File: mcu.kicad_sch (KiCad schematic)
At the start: 37 parts, among them J17 CAN, J19 Conn_ARM_JTAG_SWD_10, J20 Conn_ARM_JTAG_SWD_10, J21 Conn_01x04_Pin, SW1 RESET, SW2 BOOT, U17 HDC1080, U18 SN65HVD230, U8 STM32G473CBTx, Y1 8 MHz

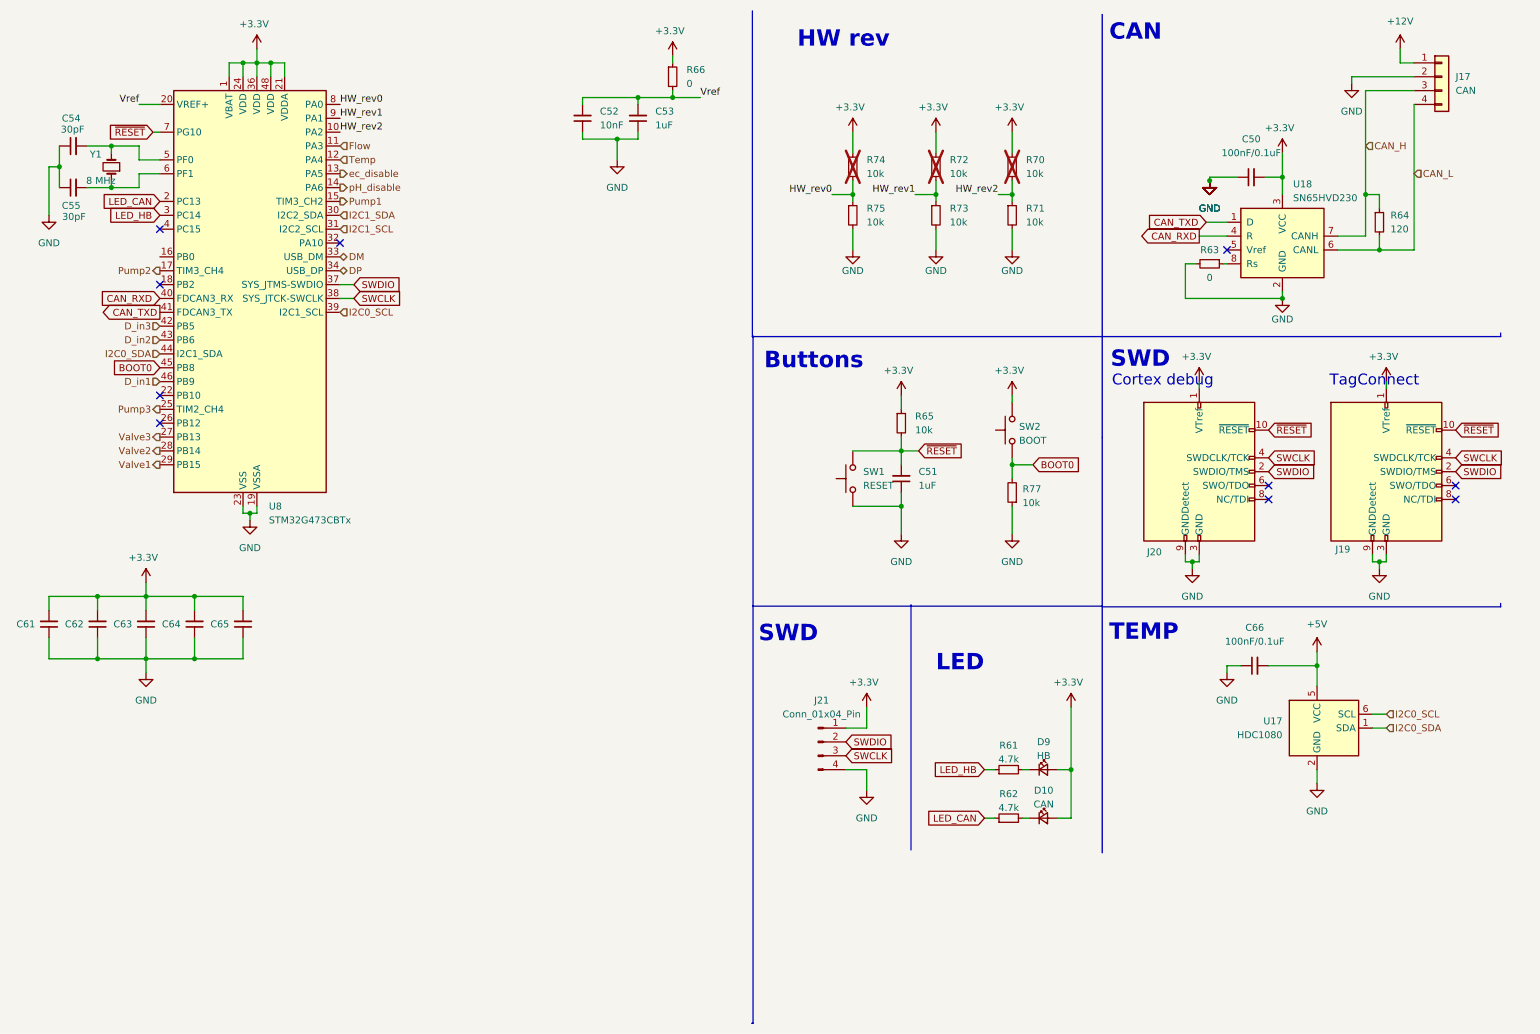
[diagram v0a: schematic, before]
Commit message: Fix ERC warnings
See #28
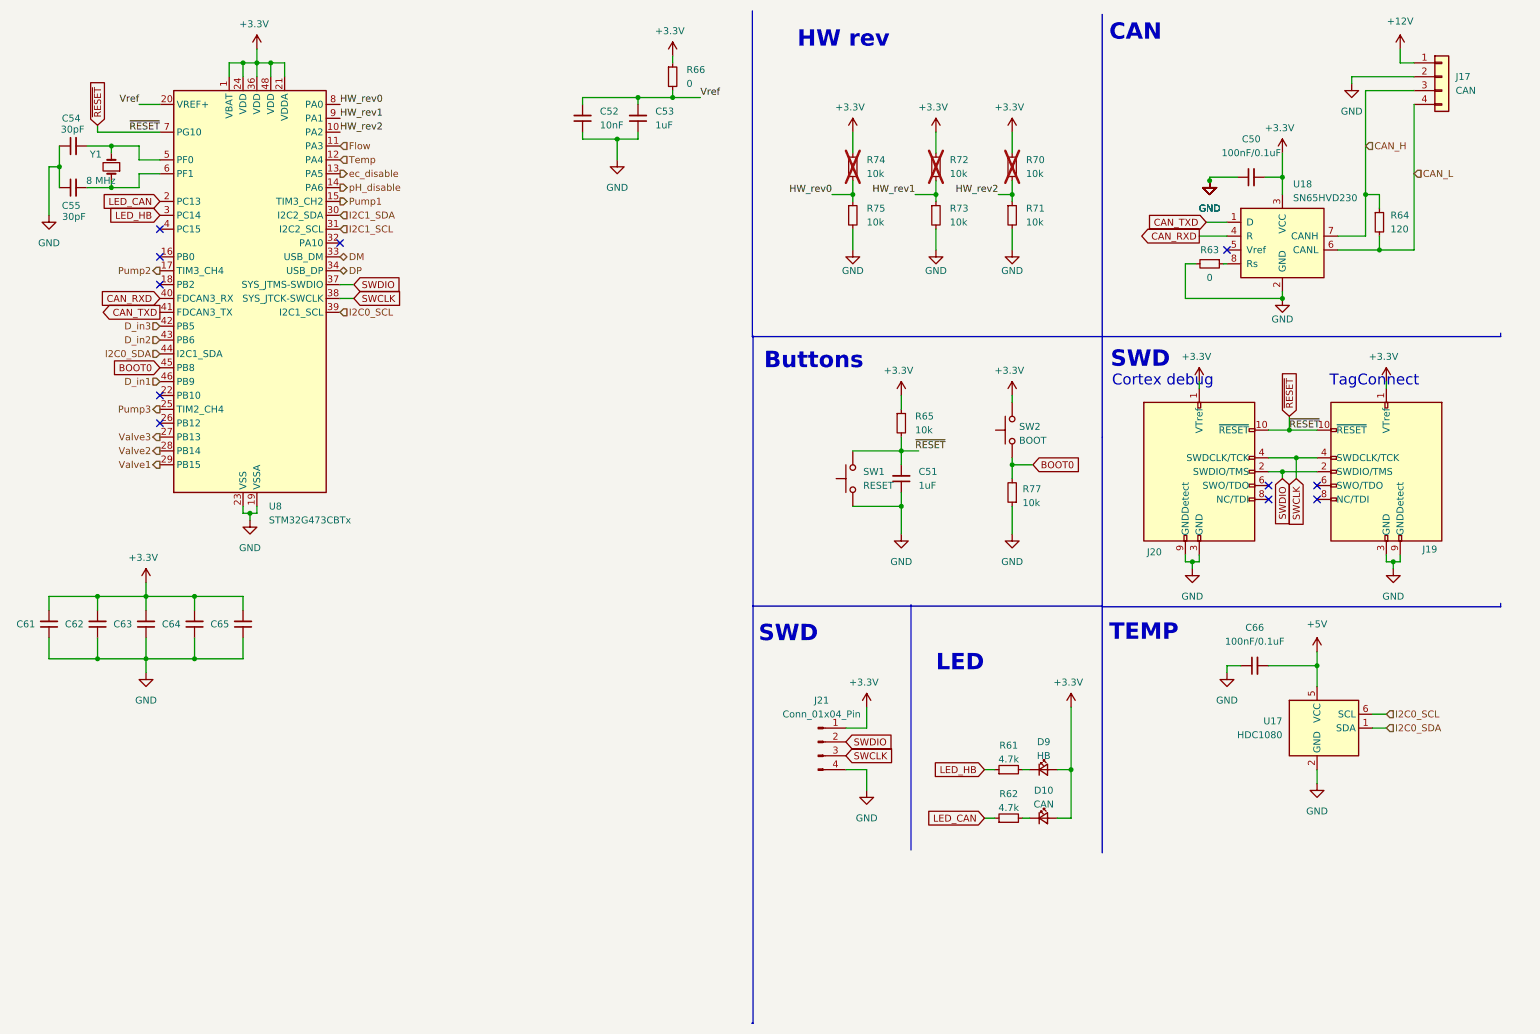
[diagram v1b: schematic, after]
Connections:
- no-connect marks 10 -> 11
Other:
- moved on the sheet: J19

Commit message: Fix ERC errors
Closes #28
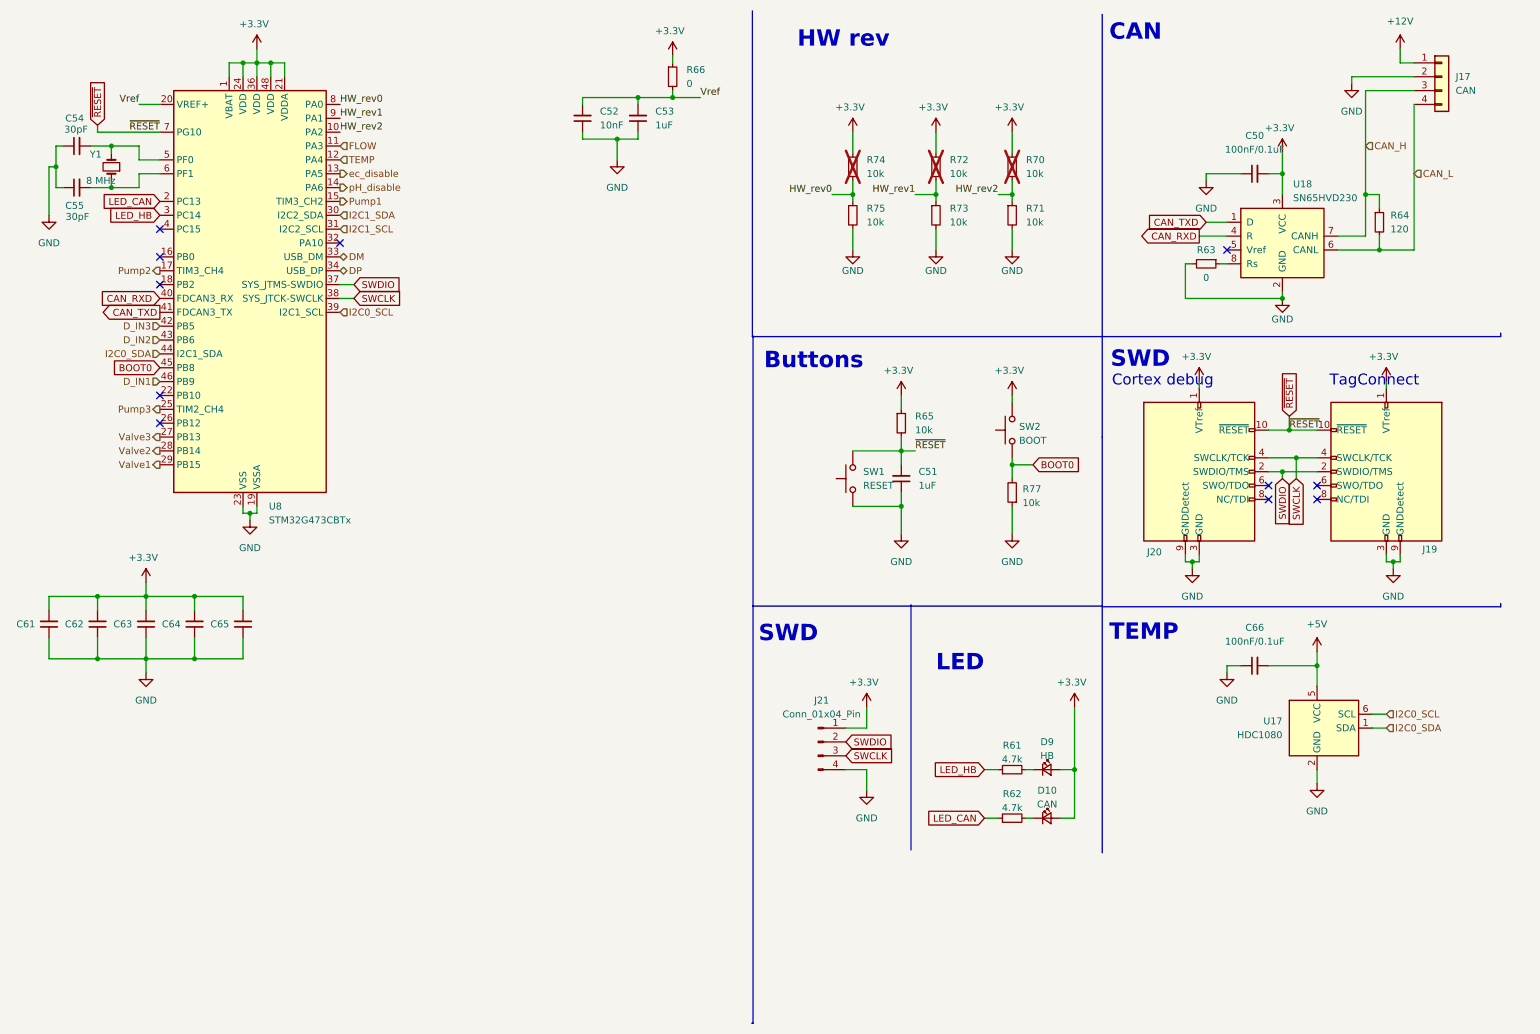
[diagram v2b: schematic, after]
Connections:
- net D_in1 renamed D_IN1
- net D_in2 renamed D_IN2
- net D_in3 renamed D_IN3
- net Flow renamed FLOW
- net Temp renamed TEMP
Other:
- moved on the sheet: C50, C54, C55, D10, D9, R61, R62, R63

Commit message: Bump HW rev
Closes #43
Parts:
- R74: now fitted; now in the parts list
- R75: now not fitted; now left out of the parts list
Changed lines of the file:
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@@
 		(unit 1)
 		(exclude_from_sim no)
-		(in_bom no)
-		(on_board yes)
-		(dnp yes)
+		(in_bom yes)
+		(on_board yes)
+		(dnp no)
 		(fields_autoplaced yes)
 		(property "Reference" "R74"
@@
 		(unit 1)
 		(exclude_from_sim no)
-		(in_bom yes)
-		(on_board yes)
-		(dnp no)
+		(in_bom no)
+		(on_board yes)
+		(dnp yes)
 		(fields_autoplaced yes)
 		(property "Reference" "R75"

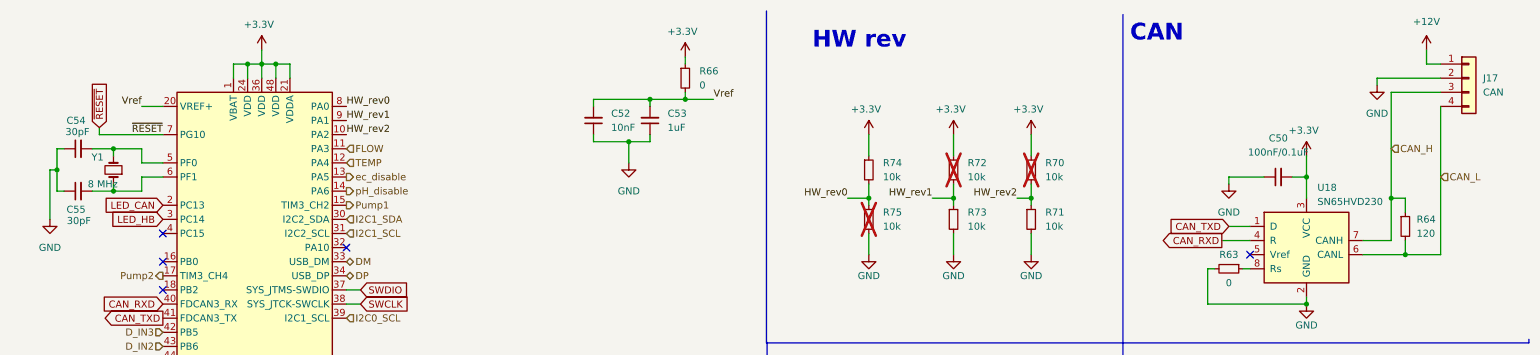
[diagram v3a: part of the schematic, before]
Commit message: Add testpoints
Closes #47
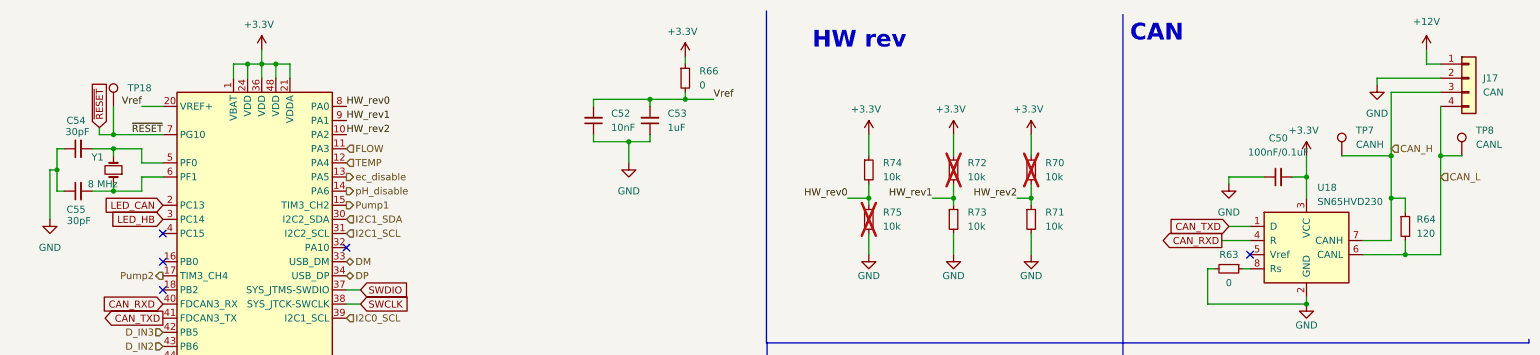
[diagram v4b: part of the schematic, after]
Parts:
- added TP18: Reset, TestPoint:TestPoint_Pad_D1.5mm, symbol Connector:TestPoint
- added TP7: CANH, TestPoint:TestPoint_Pad_D1.5mm, symbol Connector:TestPoint
- added TP8: CANL, TestPoint:TestPoint_Pad_D1.5mm, symbol Connector:TestPoint
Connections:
- net CAN_H: now also TP7.1
- net CAN_L: now also TP8.1
- net ~{RESET}: now also TP18.1

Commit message: Update manufacturing positions and rotations of parts
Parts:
- J17: JLCPCB Position Offset (none) -> 0.5,3.5
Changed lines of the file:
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@@
+			)
+		)
+		(property "JLCPCB Position Offset" "0.5,3.5"
+			(at 274.32 24.13 0)
+			(effects
+				(font
+					(size 1.27 1.27)
+				)
+				(hide yes)
 			)
 		)

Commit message: Include THT components in manufacturing
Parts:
- J17, J20: now in the parts list
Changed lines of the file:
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@@
 		(unit 1)
 		(exclude_from_sim no)
-		(in_bom no)
+		(in_bom yes)
 		(on_board yes)
 		(dnp no)
@@
 		(unit 1)
 		(exclude_from_sim no)
-		(in_bom no)
-		(on_board yes)
-		(dnp no)
+		(in_bom yes)
+		(on_board yes)
+		(dnp no)
